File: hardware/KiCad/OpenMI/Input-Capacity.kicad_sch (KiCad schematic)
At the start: 8 parts

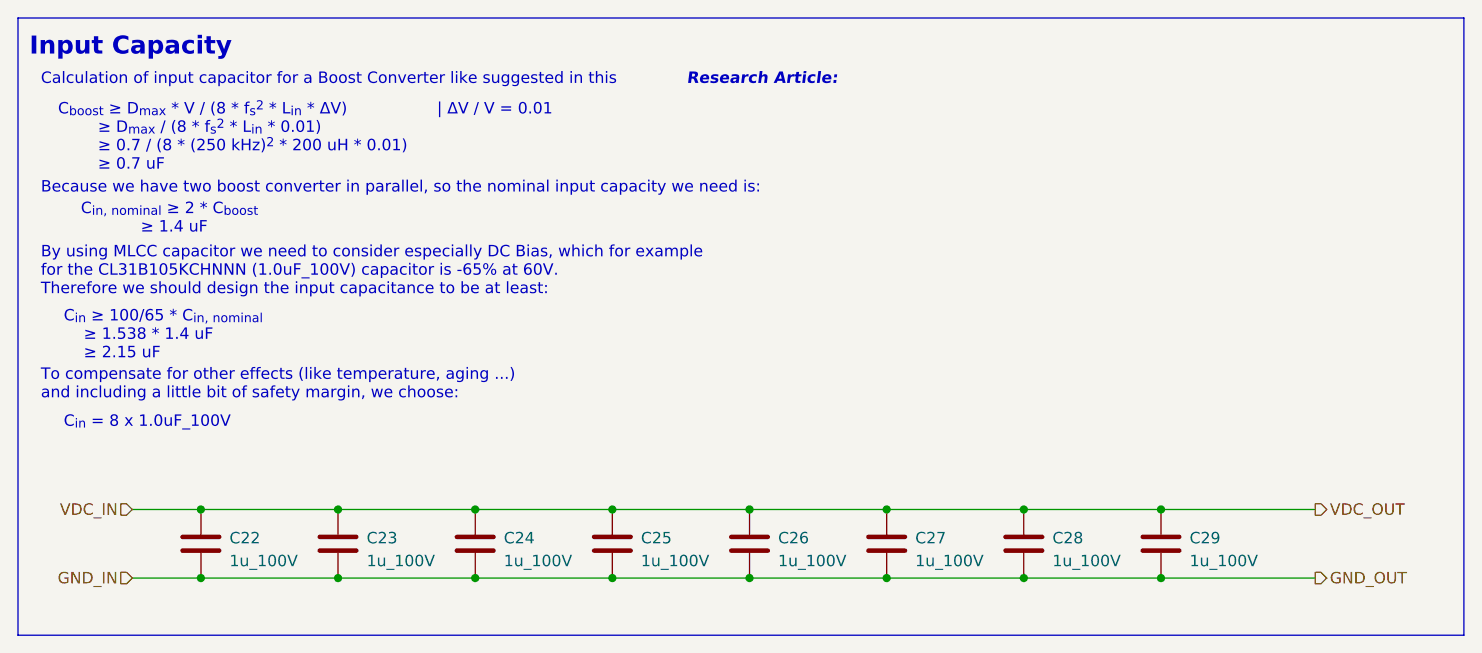
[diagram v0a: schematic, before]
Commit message: chore(hw): updates project to KiCad 8
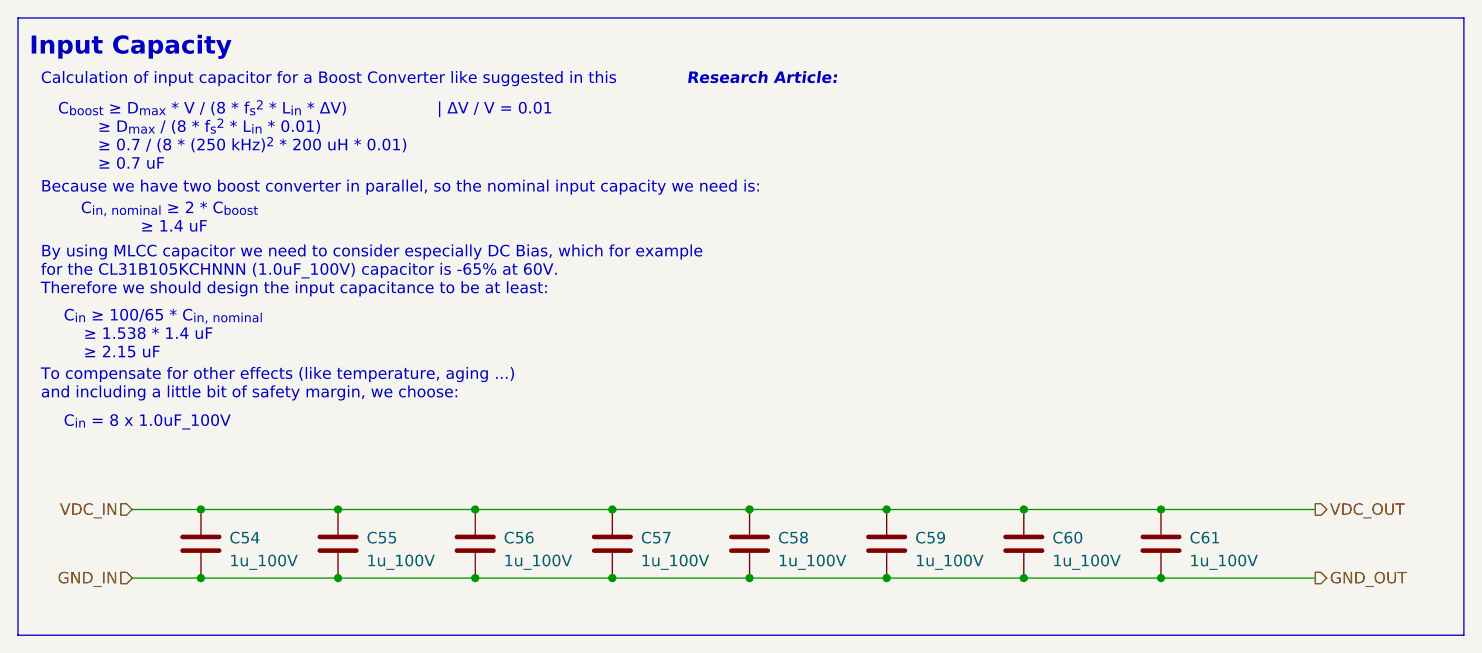
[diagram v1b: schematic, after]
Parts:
- renumbered C22 to C54, C23 to C55, C24 to C56, C25 to C57, C26 to C58, C27 to C59, C28 to C60, C29 to C61
